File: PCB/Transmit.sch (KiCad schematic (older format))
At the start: 25 parts, among them U14 TSX9291, U15 LTC6090-5, U16 AD5450, U17 ADA4522-1

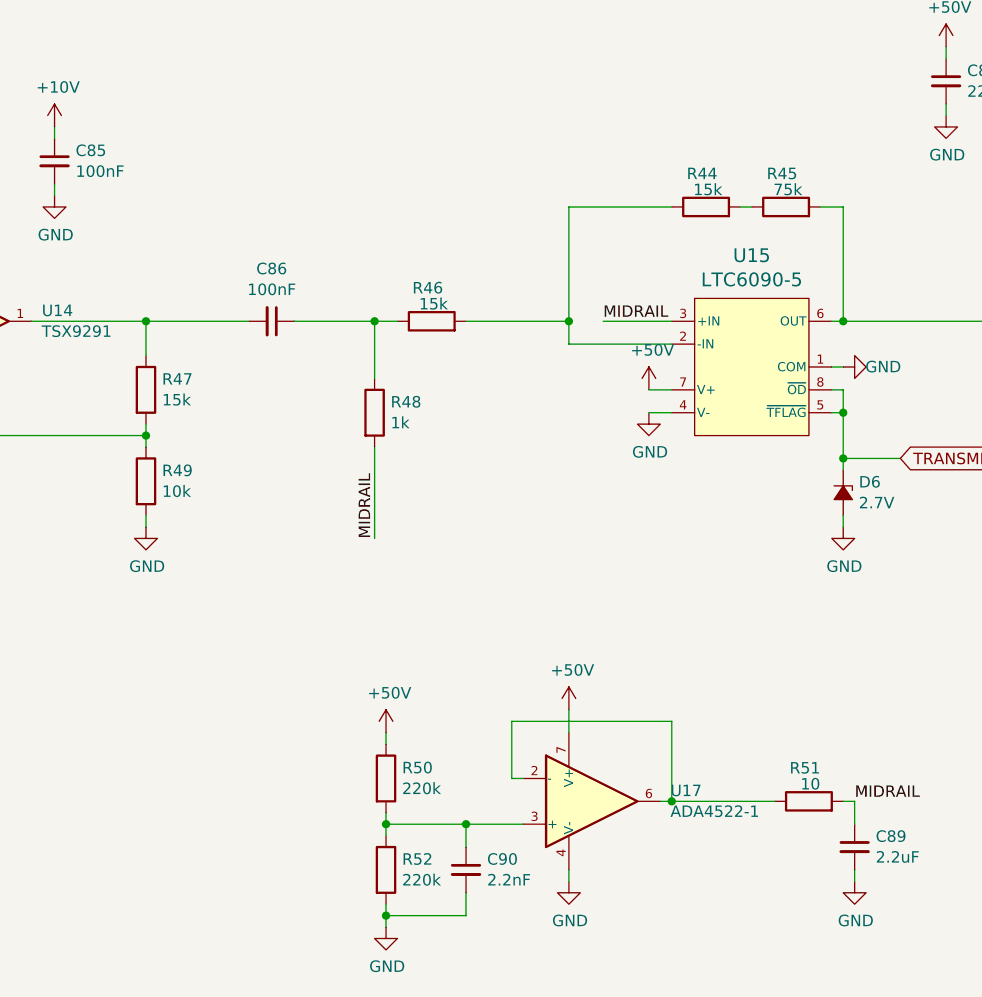
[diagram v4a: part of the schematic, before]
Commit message: Remove unnecessary series resistors, rearrange connections on FPGA and microcontroller, rearrange debug pins, layout most of FPGA and microcontroller sections
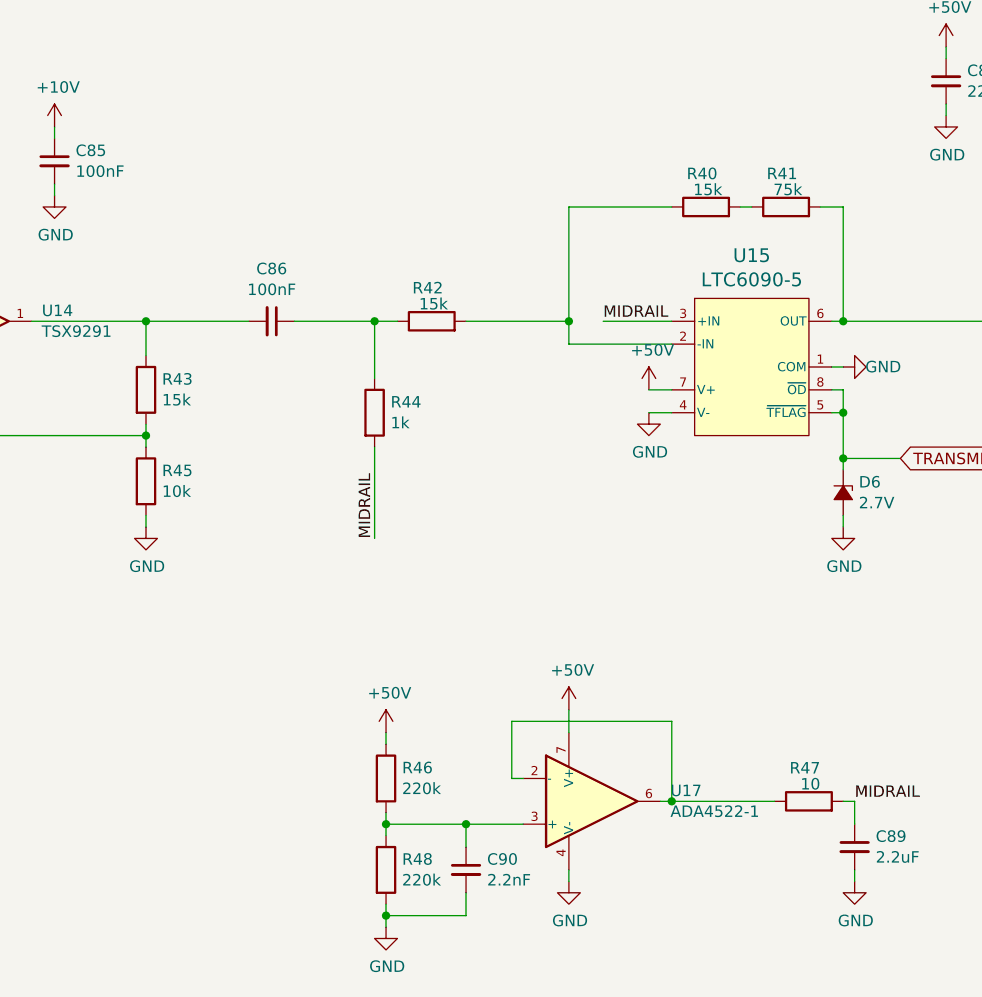
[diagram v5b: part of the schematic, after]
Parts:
- renumbered R44 to R40, R45 to R41, R46 to R42, R47 to R43, R48 to R44, R49 to R45, R50 to R46, R51 to R47, R52 to R48
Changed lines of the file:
@@
 $EndComp
 $Comp
-L power:GND #PWR0144
+L power:GND #PWR0143
 U 1 1 5DE63ED6
 P 2750 4100
-F 0 "#PWR0144" H 2750 3850 50  0001 C CNN
+F 0 "#PWR0143" H 2750 3850 50  0001 C CNN
 F 1 "GND" H 2755 3927 50  0000 C CNN
 F 2 "" H 2750 4100 50  0001 C CNN
@@
 $EndComp
 $Comp
-L Parts:+50V #PWR0141
+L Parts:+50V #PWR0140
 U 1 1 5DEC98C8
 P 6800 3900
-F 0 "#PWR0141" H 6800 3750 50  0001 C CNN
+F 0 "#PWR0140" H 6800 3750 50  0001 C CNN
 F 1 "+50V" H 6815 4073 50  0000 C CNN
 F 2 "" H 6800 3900 50  0001 C CNN
@@
 	6800 3900 6900 3900
 $Comp
-L power:GND #PWR0143
+L power:GND #PWR0142
 U 1 1 5DECB29F
 P 6800 4000
-F 0 "#PWR0143" H 6800 3750 50  0001 C CNN
+F 0 "#PWR0142" H 6800 3750 50  0001 C CNN
 F 1 "GND" H 6805 3827 50  0000 C CNN
 F 2 "" H 6800 4000 50  0001 C CNN
@@
 $EndComp
 $Comp
-L power:GND #PWR0142
+L power:GND #PWR0141
 U 1 1 5DED523B
 P 3700 3950
-F 0 "#PWR0142" H 3700 3700 50  0001 C CNN
+F 0 "#PWR0141" H 3700 3700 50  0001 C CNN
 F 1 "GND" H 3705 3777 50  0000 C CNN
 F 2 "" H 3700 3950 50  0001 C CNN
@@
 $EndComp
 $Comp
-L Device:R R49
+L Device:R R45
 U 1 1 5DEDD2CE
 P 4600 4300
-F 0 "R49" H 4670 4346 50  0000 L CNN
+F 0 "R45" H 4670 4346 50  0000 L CNN
 F 1 "10k" H 4670 4255 50  0000 L CNN
 F 2 "Resistors_SMD:R_0603_HandSoldering" V 4530 4300 50  0001 C CNN
@@
 $EndComp
 $Comp
-L power:GND #PWR0145
+L power:GND #PWR0144
 U 1 1 5DEDEBA9
 P 4600 4500
-F 0 "#PWR0145" H 4600 4250 50  0001 C CNN
+F 0 "#PWR0144" H 4600 4250 50  0001 C CNN
 F 1 "GND" H 4605 4327 50  0000 C CNN
 F 2 "" H 4600 4500 50  0001 C CNN
@@
 $EndComp
 $Comp
-L Device:R R47
+L Device:R R43
 U 1 1 5DEDF69F
 P 4600 3900
-F 0 "R47" H 4670 3946 50  0000 L CNN
+F 0 "R43" H 4670 3946 50  0000 L CNN
 F 1 "15k" H 4670 3855 50  0000 L CNN
 F 2 "Resistors_SMD:R_0603_HandSoldering" V 4530 3900 50  0001 C CNN
@@
 $EndComp
 $Comp
-L Device:R R46
+L Device:R R42
 U 1 1 5DED8CA3
 P 5850 3600
-F 0 "R46" V 5995 3550 50  0000 L CNN
+F 0 "R42" V 5995 3550 50  0000 L CNN
 F 1 "15k" V 5925 3529 50  0000 L CNN
 F 2 "Resistors_SMD:R_0603_HandSoldering" V 5780 3600 50  0001 C CNN
@@
 $EndComp
 $Comp
-L Device:R R45
+L Device:R R41
 U 1 1 5DEE04B6
 P 7400 3100
-F 0 "R45" V 7545 3050 50  0000 L CNN
+F 0 "R41" V 7545 3050 50  0000 L CNN
 F 1 "75k" V 7475 3029 50  0000 L CNN
 F 2 "Resistors_SMD:R_0603_HandSoldering" V 7330 3100 50  0001 C CNN
@@
 $EndComp
 $Comp
-L Device:R R44
+L Device:R R40
 U 1 1 5DEE0B32
 P 7050 3100
-F 0 "R44" V 7195 3050 50  0000 L CNN
+F 0 "R40" V 7195 3050 50  0000 L CNN
 F 1 "15k" V 7125 3029 50  0000 L CNN
 F 2 "Resistors_SMD:R_0603_HandSoldering" V 6980 3100 50  0001 C CNN
@@
 	8500 3800 8550 3800
 $Comp
-L Device:R R51
+L Device:R R47
 U 1 1 5DF0A2F8
 P 7500 5700
-F 0 "R51" V 7645 5650 50  0000 L CNN
+F 0 "R47" V 7645 5650 50  0000 L CNN
 F 1 "10" V 7575 5650 50  0000 L CNN
 F 2 "Resistors_SMD:R_0603_HandSoldering" V 7430 5700 50  0001 C CNN
@@
 $EndComp
 $Comp
-L Parts:+50V #PWR0147
+L Parts:+50V #PWR0146
 U 1 1 5DF12D05
 P 6450 5300
-F 0 "#PWR0147" H 6450 5150 50  0001 C CNN
+F 0 "#PWR0146" H 6450 5150 50  0001 C CNN
 F 1 "+50V" H 6465 5473 50  0000 C CNN
 F 2 "" H 6450 5300 50  0001 C CNN
@@
 	6450 5300 6450 5400
 $Comp
-L power:GND #PWR0151
+L power:GND #PWR0150
 U 1 1 5DF13CC4
 P 6450 6050
-F 0 "#PWR0151" H 6450 5800 50  0001 C CNN
+F 0 "#PWR0150" H 6450 5800 50  0001 C CNN
 F 1 "GND" H 6455 5877 50  0000 C CNN
 F 2 "" H 6450 6050 50  0001 C CNN
@@
 	6900 5700 7350 5700
 $Comp
-L Device:R R50
+L Device:R R46
 U 1 1 5DF1EF50
 P 5650 5600
-F 0 "R50" H 5720 5646 50  0000 L CNN
+F 0 "R46" H 5720 5646 50  0000 L CNN
 F 1 "220k" H 5720 5555 50  0000 L CNN
 F 2 "Resistors_SMD:R_0603_HandSoldering" V 5580 5600 50  0001 C CNN
@@
 $EndComp
 $Comp
-L Device:R R52
+L Device:R R48
 U 1 1 5DF1F6B1
 P 5650 6000
-F 0 "R52" H 5720 6046 50  0000 L CNN
+F 0 "R48" H 5720 6046 50  0000 L CNN
 F 1 "220k" H 5720 5955 50  0000 L CNN
 F 2 "Resistors_SMD:R_0603_HandSoldering" V 5580 6000 50  0001 C CNN
@@
 $EndComp
 $Comp
-L power:GND #PWR0152
+L power:GND #PWR0151
 U 1 1 5DF23E71
 P 7700 6050
-F 0 "#PWR0152" H 7700 5800 50  0001 C CNN
+F 0 "#PWR0151" H 7700 5800 50  0001 C CNN
 F 1 "GND" H 7705 5877 50  0000 C CNN
 F 2 "" H 7700 6050 50  0001 C CNN
@@
 $EndComp
 $Comp
-L power:GND #PWR0133
+L power:GND #PWR0132
 U 1 1 5DF28C27
 P 8100 2700
-F 0 "#PWR0133" H 8100 2450 50  0001 C CNN
+F 0 "#PWR0132" H 8100 2450 50  0001 C CNN
 F 1 "GND" H 8105 2527 50  0000 C CNN
 F 2 "" H 8100 2700 50  0001 C CNN
@@
 $EndComp
 $Comp
-L Parts:+50V #PWR0131
+L Parts:+50V #PWR0130
 U 1 1 5DF2926F
 P 8100 2400
-F 0 "#PWR0131" H 8100 2250 50  0001 C CNN
+F 0 "#PWR0130" H 8100 2250 50  0001 C CNN
 F 1 "+50V" H 8115 2573 50  0000 C CNN
 F 2 "" H 8100 2400 50  0001 C CNN
@@
 	8100 2650 8100 2700
 $Comp
-L power:GND #PWR0153
+L power:GND #PWR0152
 U 1 1 5DF2F3AB
 P 5650 6250
-F 0 "#PWR0153" H 5650 6000 50  0001 C CNN
+F 0 "#PWR0152" H 5650 6000 50  0001 C CNN
 F 1 "GND" H 5655 6077 50  0000 C CNN
 F 2 "" H 5650 6250 50  0001 C CNN
@@
 $EndComp
 $Comp
-L Parts:+50V #PWR0148
+L Parts:+50V #PWR0147
 U 1 1 5DF2F9A4
 P 5650 5400
-F 0 "#PWR0148" H 5650 5250 50  0001 C CNN
+F 0 "#PWR0147" H 5650 5250 50  0001 C CNN
 F 1 "+50V" H 5665 5573 50  0000 C CNN
 F 2 "" H 5650 5400 50  0001 C CNN
@@
 MIDRAIL
 $Comp
-L Device:R R48
+L Device:R R44
 U 1 1 5DF444B8
 P 5600 4000
-F 0 "R48" H 5670 4046 50  0000 L CNN
+F 0 "R44" H 5670 4046 50  0000 L CNN
 F 1 "1k" H 5670 3955 50  0000 L CNN
 F 2 "Resistors_SMD:R_0603_HandSoldering" V 5530 4000 50  0001 C CNN
@@
 	5250 3600 5600 3600
 $Comp
-L power:GND #PWR0139
+L power:GND #PWR0138
 U 1 1 5DF769F2
 P 7650 3800
-F 0 "#PWR0139" H 7650 3550 50  0001 C CNN
+F 0 "#PWR0138" H 7650 3550 50  0001 C CNN
 F 1 "GND" V 7650 3625 50  0000 C CNN
 F 2 "" H 7650 3800 50  0001 C CNN
@@
 $EndComp
 $Comp
-L power:GND #PWR0146
+L power:GND #PWR0145
 U 1 1 5DF7E3C9
 P 7650 4500
-F 0 "#PWR0146" H 7650 4250 50  0001 C CNN
+F 0 "#PWR0145" H 7650 4250 50  0001 C CNN
 F 1 "GND" H 7655 4327 50  0000 C CNN
 F 2 "" H 7650 4500 50  0001 C CNN
@@
 $EndComp
 $Comp
-L power:GND #PWR0150
+L power:GND #PWR0149
 U 1 1 5DFB3BBB
 P 8650 5850
-F 0 "#PWR0150" H 8650 5600 50  0001 C CNN
+F 0 "#PWR0149" H 8650 5600 50  0001 C CNN
 F 1 "GND" H 8655 5677 50  0000 C CNN
 F 2 "" H 8650 5850 50  0001 C CNN
@@
 $EndComp
 $Comp
-L Parts:+50V #PWR0149
+L Parts:+50V #PWR0148
 U 1 1 5DFB3BC5
 P 8650 5550
-F 0 "#PWR0149" H 8650 5400 50  0001 C CNN
+F 0 "#PWR0148" H 8650 5400 50  0001 C CNN
 F 1 "+50V" H 8665 5723 50  0000 C CNN
 F 2 "" H 8650 5550 50  0001 C CNN
@@
 	8650 5800 8650 5850
 $Comp
-L power:GND #PWR0136
+L power:GND #PWR0135
 U 1 1 5E3B7B63
 P 800 3100
-F 0 "#PWR0136" H 800 2850 50  0001 C CNN
+F 0 "#PWR0135" H 800 2850 50  0001 C CNN
 F 1 "GND" H 805 2927 50  0000 C CNN
 F 2 "" H 800 3100 50  0001 C CNN
@@
 	800  3050 800  3100
 $Comp
-L power:+10V #PWR0137
+L power:+10V #PWR0136
 U 1 1 5E0A0743
 P 3700 3250
-F 0 "#PWR0137" H 3700 3100 50  0001 C CNN
+F 0 "#PWR0136" H 3700 3100 50  0001 C CNN
 F 1 "+10V" H 3715 3423 50  0000 C CNN
 F 2 "" H 3700 3250 50  0001 C CNN
@@
 $EndComp
 $Comp
-L power:+10V #PWR0134
+L power:+10V #PWR0133
 U 1 1 5E124B96
 P 4200 2750
-F 0 "#PWR0134" H 4200 2600 50  0001 C CNN
+F 0 "#PWR0133" H 4200 2600 50  0001 C CNN
 F 1 "+10V" H 4215 2923 50  0000 C CNN
 F 2 "" H 4200 2750 50  0001 C CNN
@@
 	4200 2750 4200 2800
 $Comp
-L power:GND #PWR0135
+L power:GND #PWR0134
 U 1 1 5E1277BF
 P 4200 3050
-F 0 "#PWR0135" H 4200 2800 50  0001 C CNN
+F 0 "#PWR0134" H 4200 2800 50  0001 C CNN
 F 1 "GND" H 4205 2877 50  0000 C CNN
 F 2 "" H 4200 3050 50  0001 C CNN
@@
 	3700 3250 3700 3300
 $Comp
-L Parts:+3V3-LN #PWR0138
+L Parts:+3V3-LN #PWR0137
 U 1 1 5E29A668
 P 1750 3700
-F 0 "#PWR0138" H 1750 3550 50  0001 C CNN
+F 0 "#PWR0137" H 1750 3550 50  0001 C CNN
 F 1 "+3V3-LN" H 1765 3873 50  0000 C CNN
 F 2 "" H 1750 3700 50  0001 C CNN
@@
 $EndComp
 $Comp
-L Parts:+3V3-LN #PWR0132
+L Parts:+3V3-LN #PWR0131
 U 1 1 5E29D33A
 P 800 2700
-F 0 "#PWR0132" H 800 2550 50  0001 C CNN
+F 0 "#PWR0131" H 800 2550 50  0001 C CNN
 F 1 "+3V3-LN" H 815 2873 50  0000 C CNN
 F 2 "" H 800 2700 50  0001 C CNN
@@
 	6450 3600 6450 3100
 $Comp
-L Parts:+3V3-LN #PWR0140
+L Parts:+3V3-LN #PWR0139
 U 1 1 5E40A399
 P 2750 3900
-F 0 "#PWR0140" H 2750 3750 50  0001 C CNN
+F 0 "#PWR0139" H 2750 3750 50  0001 C CNN
 F 1 "+3V3-LN" H 2765 4073 50  0000 C CNN
 F 2 "" H 2750 3900 50  0001 C CNN

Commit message: Fix incorrect footprint, begin organizing fabrication layer
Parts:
- C89: footprint Capacitors_SMD:C_1210_HandSoldering -> Capacitors_SMD:C_1206_HandSoldering
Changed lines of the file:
@@
 F 0 "C89" H 7792 5946 50  0000 L CNN
 F 1 "2.2uF" H 7792 5855 50  0000 L CNN
-F 2 "Capacitors_SMD:C_1210_HandSoldering" H 7700 5900 50  0001 C CNN
+F 2 "Capacitors_SMD:C_1206_HandSoldering" H 7700 5900 50  0001 C CNN
 F 3 "https://www.digikey.ca/product-detail/en/samsung-electro-mechanics/CL31A225KBHNNNE/1276-2878-1-ND/3890964" H 7700 5900 50  0001 C CNN
 	1    7700 5900
